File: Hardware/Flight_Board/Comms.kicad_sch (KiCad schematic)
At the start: 0 parts

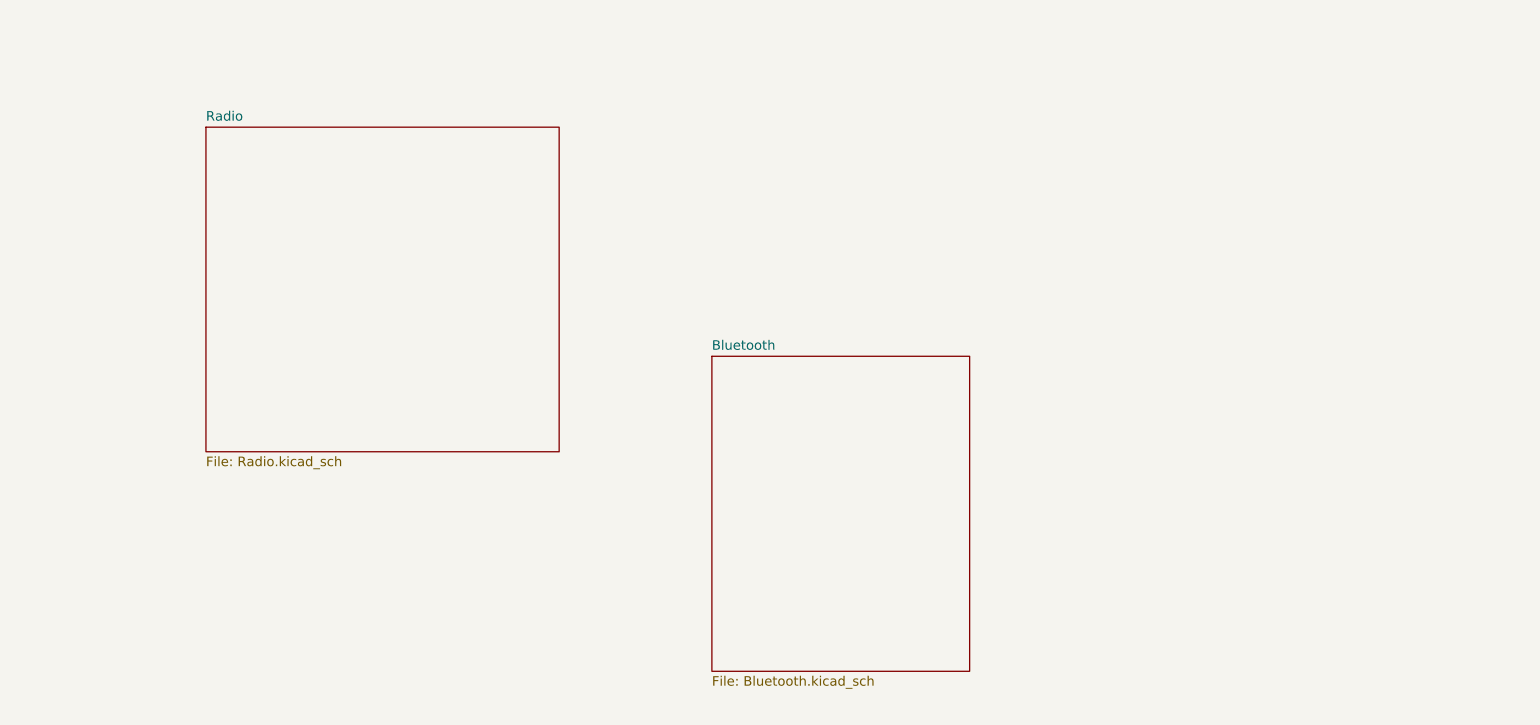
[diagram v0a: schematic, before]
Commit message: Harware GPS, Radio, Power, IMU, Barrometer Prototypes
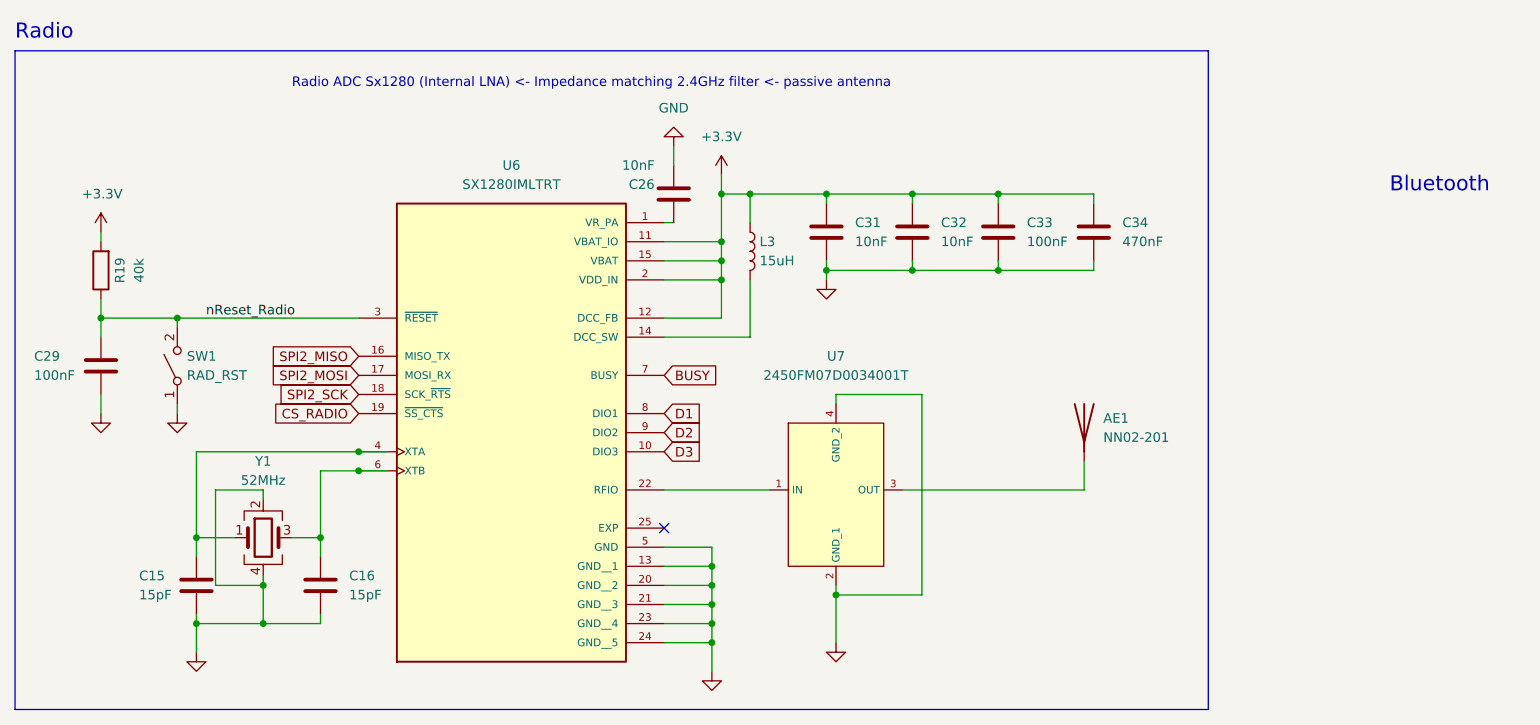
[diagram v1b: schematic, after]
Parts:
- added AE1: NN02-201, symbol Device:Antenna
- added C15, C16: 15pF, symbol Device:C
- added C26, C31, C32: 10nF, symbol Device:C
- added C29, C33: 100nF, symbol Device:C
- added C34: 470nF, symbol Device:C
- added L3: 15uH, symbol Device:L
- added R19: 40k, Resistor_SMD:R_0603_1608Metric, symbol Device:R
- added SW1: RAD_RST, symbol Switch:SW_SPST
- added U6: SX1280IMLTRT, SX1280IMLTRT:XCVR_SX1280IMLTRT, symbol RF:SX1280IMLTRT
- added U7: 2450FM07D0034001T, symbol RF_Filter:2450FM07D0034001T
- added Y1: 52MHz, https://www.mouser.com/datasheet/2/122/ECX_1637B2-2400564.pdf, symbol Device:Crystal_GND24
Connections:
- new net: C15.1, U6.4 (XTA), Y1.1
- new net: L3.2, U6.14 (DCC_SW)
- new net: C26.1, U6.1 (VR_PA)
- new net: AE1.1 (A), U7.3 (OUT)
- new net: C16.1, U6.6 (XTB), Y1.3
- new net: U6.22 (RFIO), U7.1 (IN)
- new net +3.3V: C31.1, C32.1, C33.1, C34.1, L3.1, R19.2, U6.11 (VBAT_IO), U6.12 (DCC_FB), U6.15 (VBAT), U6.2 (VDD_IN)
- new net BUSY: U6.7 (BUSY)
- new net CS_RADIO: U6.19 (~{SS_CTS})
- new net D1: U6.8 (DIO1)
- new net D2: U6.9 (DIO2)
- new net D3: U6.10 (DIO3)
- new net GND: C15.2, C16.2, C26.2, C29.2, C31.2, C32.2, C33.2, C34.2, SW1.1 (A), U6.13 (GND__1), U6.20 (GND__2), U6.21 (GND__3), U6.23 (GND__4), U6.24 (GND__5), U6.5 (GND), U7.2 (GND_1), U7.4 (GND_2), Y1.2, Y1.4
- new net SPI2_MISO: U6.16 (MISO_TX)
- new net SPI2_MOSI: U6.17 (MOSI_RX)
- new net SPI2_SCK: U6.18 (SCK_~{RTS})
- new net nReset_Radio: C29.1, R19.1, SW1.2 (B), U6.3 (~{RESET})
- no-connect marks 0 -> 1
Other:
- removed sheet Bluetooth
- removed sheet Radio
- note added: "Bluetooth"
- note added: "Radio"
- note added: "Radio ADC Sx1280 (Internal LNA) <- Impedance matching 2.4GHz filter <- passive antenna"

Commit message: ESC Rough Draft
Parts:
- added TP5: TP_RAD_RST, symbol Connector:TestPoint
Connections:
- net nReset_Radio: now also TP5.1
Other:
- note removed: "Bluetooth"
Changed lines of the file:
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@@
   (junction (at 64.77 78.74) (diameter 0) (color 0 0 0 0)
+  )
+  (junction (at 43.18 58.42) (diameter 0) (color 0 0 0 0)
   )
   (junction (at 40.64 58.42) (diameter 0) (color 0 0 0 0)
@@
     (stroke (width 0) (type default))
   )
+  (wire (pts (xy 43.18 49.53) (xy 43.18 58.42))
+    (stroke (width 0) (type default))
+  )
   (wire (pts (xy 105.41 96.52) (xy 111.76 96.52))
     (stroke (width 0) (type default))
@@
     (stroke (width 0) (type default))
   )
-  (wire (pts (xy 40.64 58.42) (xy 64.77 58.42))
+  (wire (pts (xy 40.64 58.42) (xy 43.18 58.42))
     (stroke (width 0) (type default))
   )
@@
     (stroke (width 0) (type default))
   )
+  (wire (pts (xy 43.18 58.42) (xy 64.77 58.42))
+    (stroke (width 0) (type default))
+  )
   (wire (pts (xy 138.43 52.07) (xy 138.43 50.8))
     (stroke (width 0) (type default))
@@
   )
   (text "Radio\n" (at 19.05 21.59 0)
-    (effects (font (size 2 2)) (justify left bottom))
-  )
-  (text "Bluetooth" (at 201.93 41.91 0)
     (effects (font (size 2 2)) (justify left bottom))
   )
@@
         (path "/9bcc2c41-99de-46c1-94bb-5baa5251c91c/1829169b-2de3-48c8-b2c3-f3a0e7599ed3"
           (reference "C34") (unit 1)
+        )
+      )
+    )
+  )
+  (symbol (lib_id "Connector:TestPoint") (at 43.18 49.53 0) (unit 1)
+    (in_bom yes) (on_board yes) (dnp no) (fields_autoplaced)
+    (property "Reference" "TP5" (at 45.72 44.958 0)
+      (effects (font (size 1.27 1.27)) (justify left))
+    )
+    (property "Value" "TP_RAD_RST" (at 45.72 47.498 0)
+      (effects (font (size 1.27 1.27)) (justify left))
+    )
+    (property "Footprint" "" (at 48.26 49.53 0)
+      (effects (font (size 1.27 1.27)) hide)
+    )
+    (property "Datasheet" "~" (at 48.26 49.53 0)
+      (effects (font (size 1.27 1.27)) hide)
+    )
+    (pin "1")
+    (instances
+      (project "Flight_Board"
+        (path "/9bcc2c41-99de-46c1-94bb-5baa5251c91c/a7f4894d-c2f3-4432-84fe-76ba7008892e"
+          (reference "TP5") (unit 1)
+        )
+        (path "/9bcc2c41-99de-46c1-94bb-5baa5251c91c/1829169b-2de3-48c8-b2c3-f3a0e7599ed3"
+          (reference "TP9") (unit 1)
         )
       )
@@
     )
     (pin "1")
+    (pin "2")
     (pin "3")
-    (pin "2")
     (pin "4")
     (instances
